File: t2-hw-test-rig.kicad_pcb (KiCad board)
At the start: 2 copper layers, 101.6 x 76.2 mm, 0 parts

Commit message: on to layout! and what an adventure it will be...
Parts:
- added C101: 10uF, tm-kicad-lib:SMD-0805-C, F.Cu at (25.1, 169.8)
- added C102: 100nF, tm-kicad-lib:SMD-0402-C, F.Cu at (143.9, 175.5)
- added C103: 100nF, tm-kicad-lib:SMD-0402-C, F.Cu at (141.2, 170.5)
- added C104: 100nF, tm-kicad-lib:SMD-0402-C, F.Cu at (91.8, 175.5)
- added C105: 100nF, tm-kicad-lib:SMD-0402-C, F.Cu at (126.5, 175.5)
- added C201: 100pF, tm-kicad-lib:SMD-0402-C, F.Cu at (89.2, 164.7)
- added C202: 100nF, tm-kicad-lib:SMD-0402-C, F.Cu at (68.6, 132.1)
- added C203: 100nF, tm-kicad-lib:SMD-0402-C, F.Cu at (173.6, 170.5)
- added C204: 100pF, tm-kicad-lib:SMD-0402-C, F.Cu at (105.2, 170.5)
- added C205: 10uF, tm-kicad-lib:SMD-0805-C, F.Cu at (17.4, 164.7)
- added C206: 10uF, tm-kicad-lib:SMD-0805-C, F.Cu at (16.6, 169.8)
- added C207: 100pF, tm-kicad-lib:SMD-0402-C, F.Cu at (84.1, 159.9)
- added C208: 18pF, tm-kicad-lib:SMD-0402-C, F.Cu at (66.7, 159.9)
- added C209: 100nF, tm-kicad-lib:SMD-0402-C, F.Cu at (93.4, 164.7)
- added C210: 18pF, tm-kicad-lib:SMD-0402-C, F.Cu at (42.8, 164.7)
- added C211: 100nF, tm-kicad-lib:SMD-0402-C, F.Cu at (55.1, 159.9)
- added C212: 100nF, tm-kicad-lib:SMD-0402-C, F.Cu at (49.3, 159.9)
- added C213: 10uF, tm-kicad-lib:SMD-0805-C, F.Cu at (29.3, 169.8)
- added C214: 100nF, tm-kicad-lib:SMD-0402-C, F.Cu at (43.5, 159.9)
- added C215: 100nF, tm-kicad-lib:SMD-0402-C, F.Cu at (38.5, 164.7)
- added C216: 10uF, tm-kicad-lib:SMD-0805-C, F.Cu at (37.7, 169.8)
- added C217: 100nF, tm-kicad-lib:SMD-0402-C, F.Cu at (57.0, 175.5)
- added C218: 10uF, tm-kicad-lib:SMD-0805-C, F.Cu at (20.8, 169.8)
- added C219: 10uF, tm-kicad-lib:SMD-0805-C, F.Cu at (116.8, 163.5)
- added C220: 1uF, tm-kicad-lib:SMD-0402-C, F.Cu at (63.8, 164.7)
- added C221: 1uF, tm-kicad-lib:SMD-0402-C, F.Cu at (107.3, 159.9)
- added C222: 1uF DNP, tm-kicad-lib:SMD-0402, F.Cu at (113.0, 159.9)
- added C223: 1uF DNP, tm-kicad-lib:SMD-0402, F.Cu at (118.8, 159.9)
- added C301: 10pF, tm-kicad-lib:SMD-0402-C, F.Cu at (87.6, 117.7)
- added C302: 100nF, tm-kicad-lib:SMD-0402-C, F.Cu at (86.0, 175.5)
- added C303: 100nF, tm-kicad-lib:SMD-0402-C, F.Cu at (101.5, 159.9)
- added C304: 10pF, tm-kicad-lib:SMD-0402-C, F.Cu at (89.5, 117.7)
- added C305: 100nF, tm-kicad-lib:SMD-0402-C, F.Cu at (134.0, 170.5)
- added C306: 1uF, tm-kicad-lib:SMD-0402-C, F.Cu at (138.1, 175.5)
- added C307: 100nF, tm-kicad-lib:SMD-0402-C, F.Cu at (28.0, 175.5)
- added C308: 10uF, tm-kicad-lib:SMD-0805-C, F.Cu at (41.9, 169.8)
- added C309: 10uF, tm-kicad-lib:SMD-0805-C, F.Cu at (46.1, 169.8)
- added C310: 100nF, tm-kicad-lib:SMD-0402-C, F.Cu at (55.4, 164.7)
- added C311: 100nF, tm-kicad-lib:SMD-0402-C, F.Cu at (101.8, 164.7)
- added C312: 10uF, tm-kicad-lib:SMD-0805-C, F.Cu at (121.0, 163.5)
- added C313: 100nF, tm-kicad-lib:SMD-0402-C, F.Cu at (148.4, 170.5)
- added C314: 100nF, tm-kicad-lib:SMD-0402-C, F.Cu at (53.4, 169.9)
- added C401: 100nF, tm-kicad-lib:SMD-0402-C, F.Cu at (108.8, 170.5)
- added C402: 100nF, tm-kicad-lib:SMD-0402-C, F.Cu at (148.0, 90.2)
- added C403: 100nF, tm-kicad-lib:SMD-0402-C, F.Cu at (97.6, 175.5)
- added C404: 100nF, tm-kicad-lib:SMD-0402-C, F.Cu at (147.3, 86.4)
- added C405: 100pF, tm-kicad-lib:SMD-0402-C, F.Cu at (115.0, 175.5)
- added C406: 100pF, tm-kicad-lib:SMD-0402-C, F.Cu at (147.3, 85.1)
- added C407: 100nF, tm-kicad-lib:SMD-0402-C, F.Cu at (106.0, 162.2)
- added C408: 100nF, tm-kicad-lib:SMD-0402-C, F.Cu at (80.7, 164.7)
- added C409: 100nF, tm-kicad-lib:SMD-0402-C, F.Cu at (76.5, 164.7)
- added C410: 100nF, tm-kicad-lib:SMD-0402-C, F.Cu at (84.9, 164.7)
- added C411: 100pF, tm-kicad-lib:SMD-0402-C, F.Cu at (62.8, 175.5)
- added C412: 100pF, tm-kicad-lib:SMD-0402-C, F.Cu at (132.3, 175.5)
- added C413: 100nF, tm-kicad-lib:SMD-0402-C, F.Cu at (45.4, 175.5)
- added C414: 100nF, tm-kicad-lib:SMD-0402-C, F.Cu at (51.2, 164.7)
- added C415: 100pF, tm-kicad-lib:SMD-0402-C, F.Cu at (39.6, 175.5)
- added C501: 100nF, tm-kicad-lib:SMD-0402-C, F.Cu at (137.6, 170.5)
- added C502: 100nF, tm-kicad-lib:SMD-0402-C, F.Cu at (130.4, 170.5)
- added C503: 100pF, tm-kicad-lib:SMD-0402-C, F.Cu at (22.2, 175.5)
- added C504: 100nF, tm-kicad-lib:SMD-0402-C, F.Cu at (16.4, 175.5)
- added C505: 100nF, tm-kicad-lib:SMD-0402-C, F.Cu at (109.2, 175.5)
- added C506: 100pF, tm-kicad-lib:SMD-0402-C, F.Cu at (72.3, 164.7)
- added C507: 100nF, tm-kicad-lib:SMD-0402-C, F.Cu at (60.9, 159.9)
- added C508: 100nF, tm-kicad-lib:SMD-0402-C, F.Cu at (33.8, 175.5)
- added C509: 100pF, tm-kicad-lib:SMD-0402-C, F.Cu at (68.1, 164.7)
- added D201: PRTR5V0U2X,215, tm-kicad-lib:PRTR5V0U2X,215, F.Cu at (77.7, 131.3)
- added D202: PRTR5V0U2X,215, tm-kicad-lib:PRTR5V0U2X,215, F.Cu at (74.4, 131.3)
- added D203: PRTR5V0U2X,215, tm-kicad-lib:PRTR5V0U2X,215, F.Cu at (73.9, 83.8)
- added D301: BLUE, LEDs:LED-0603, F.Cu at (114.3, 144.8)
- added D302: YELLOW, LEDs:LED-0603, F.Cu at (120.7, 144.8)
- added D303: GREEN, LEDs:LED-0603, F.Cu at (127.0, 144.8)
- added D304: RED, LEDs:LED-0603, F.Cu at (133.3, 144.8)
- added H101: M2.5, tm-kicad-lib:MountingHole_2-5mm, F.Cu at (147.3, 132.1)
- added H102: M2.5, tm-kicad-lib:MountingHole_2-5mm, F.Cu at (83.8, 78.7)
- added H103: M2.5, tm-kicad-lib:MountingHole_2-5mm, F.Cu at (147.3, 78.7)
- added H104: M2.5, tm-kicad-lib:MountingHole_2-5mm, F.Cu at (94.1, 118.9)
- added H105: M2.5, tm-kicad-lib:MountingHole_2-5mm, F.Cu at (53.3, 78.7)
- added H106: M2.5, tm-kicad-lib:MountingHole_2-5mm, F.Cu at (53.3, 149.9)
- added J101: CONN_01X02, Pin_Headers:Pin_Header_Straight_1x02, F.Cu at (54.0, 92.1)
- added J102: BARREL_JACK, Connect:BARREL_JACK, F.Cu at (61.0, 82.5)
- added J103: CONN_01X02, Pin_Headers:Pin_Header_Straight_1x02, F.Cu at (67.9, 88.3)
- added J201: MICROUSB-TH, tm-kicad-lib:Seeed-USB-Micro-320010028, F.Cu at (73.7, 77.5)
- added J202: CONN_01X02, Pin_Headers:Pin_Header_Straight_1x02, F.Cu at (78.1, 83.2)
- added J203: USB_A_2_stack, tm-kicad-lib:Molex-0672983090, F.Cu at (63.7, 138.2)
- added J204: USB_A_TH, tm-kicad-lib:USB-A, F.Cu at (58.4, 125.5)
- added J301: CONN_02x05, 0.05", tm-kicad-lib:CONN_02x05_0.05in, F.Cu at (77.5, 122.6)
- added L201: BLM21PG221SN1D, tm-kicad-lib:SMD-0805-R, F.Cu at (66.0, 132.1)
- added L202: BLM21PG221SN1D, tm-kicad-lib:SMD-0805-R, F.Cu at (62.2, 130.2)
- added L301: 10uH, tm-kicad-lib:SMD-0603-R, F.Cu at (137.6, 162.2)
- added L401: 10uH, tm-kicad-lib:SMD-0603-R, F.Cu at (141.8, 162.2)
- added L402: 10uH, tm-kicad-lib:SMD-0603-R, F.Cu at (147.3, 88.3)
- added L403: 10uH, tm-kicad-lib:SMD-0603-R, F.Cu at (25.9, 164.7)
- added L404: 10uH, tm-kicad-lib:SMD-0603-R, F.Cu at (30.1, 164.7)
- added L405: 10uH, tm-kicad-lib:SMD-0603-R, F.Cu at (146.0, 162.2)
- added L501: 10uH, tm-kicad-lib:SMD-0603-R, F.Cu at (21.7, 164.7)
- added L502: 10uH, tm-kicad-lib:SMD-0603-R, F.Cu at (34.3, 164.7)
- added L503: 10uH, tm-kicad-lib:SMD-0603-R, F.Cu at (133.4, 162.2)
- added Q101: pMOS, Housings_SOT-23_SOT-143_TSOT-6:SOT-23, F.Cu at (69.2, 83.8)
- added Q401: CJ2302, Housings_SOT-23_SOT-143_TSOT-6:SOT-23, F.Cu at (128.5, 96.0)
- added Q402: CJ2302, Housings_SOT-23_SOT-143_TSOT-6:SOT-23, F.Cu at (134.6, 83.8)
- added Q403: CJ2302, Housings_SOT-23_SOT-143_TSOT-6:SOT-23, F.Cu at (137.9, 104.4)
- added Q404: CJ2302, Housings_SOT-23_SOT-143_TSOT-6:SOT-23, F.Cu at (104.4, 82.0)
- added R201: 100kR, tm-kicad-lib:SMD-0402-R, F.Cu at (80.2, 175.5)
- added R202: 100kR, tm-kicad-lib:SMD-0402-R, F.Cu at (155.6, 170.5)
- added R203: 0R DNP, tm-kicad-lib:SMD-0603, F.Cu at (70.5, 128.3)
- added R204: 0R DNP, tm-kicad-lib:SMD-0603, F.Cu at (50.4, 169.8)
- added R205: 100kR, tm-kicad-lib:SMD-0402-R, F.Cu at (68.6, 175.5)
- added R206: 100kR, tm-kicad-lib:SMD-0402-R, F.Cu at (78.3, 159.9)
- added R207: 10kR, tm-kicad-lib:SMD-0402-R, F.Cu at (126.8, 170.5)
- added R208: 10kR, tm-kicad-lib:SMD-0402-R, F.Cu at (97.6, 164.7)
- added R209: 2.7kR 1%, tm-kicad-lib:SMD-0402-R, F.Cu at (124.6, 159.9)
- added R210: 1MR, tm-kicad-lib:SMD-0402-R, F.Cu at (59.6, 164.7)
- added R211: 1MR, tm-kicad-lib:SMD-0402-R, F.Cu at (31.9, 159.9)
- added R212: 1MR, tm-kicad-lib:SMD-0402-R, F.Cu at (112.4, 170.5)
- added R213: 1MR, tm-kicad-lib:SMD-0402-R, F.Cu at (72.5, 159.9)
- added R301: 1kR, tm-kicad-lib:SMD-0402-R, F.Cu at (103.4, 175.5)
- added R302: 330R, tm-kicad-lib:SMD-0402-R, F.Cu at (170.0, 170.5)
- added R303: 120R, tm-kicad-lib:SMD-0402-R, F.Cu at (149.7, 175.5)
- added R304: 1kR, tm-kicad-lib:SMD-0402-R, F.Cu at (74.4, 175.5)
- added R305: 10kR, tm-kicad-lib:SMD-0402-R, F.Cu at (110.3, 162.2)
- added R306: 10kR, tm-kicad-lib:SMD-0402-R, F.Cu at (153.2, 166.4)
- added R307: 10kR, tm-kicad-lib:SMD-0402-R, F.Cu at (152.0, 170.5)
- added R308: 1kR, tm-kicad-lib:SMD-0402-R, F.Cu at (51.2, 175.5)
- added R309: 1kR, tm-kicad-lib:SMD-0402-R, F.Cu at (162.8, 170.5)
- added R310: 10kR, tm-kicad-lib:SMD-0402-R, F.Cu at (95.7, 159.9)
- added R401: 10kR, tm-kicad-lib:SMD-0402-R, F.Cu at (47.0, 164.7)
- added R402: 10kR, tm-kicad-lib:SMD-0402-R, F.Cu at (37.7, 159.9)
- added R403: 20mR 1%, Resistors_SMD:R_1206, F.Cu at (132.1, 96.5)
- added R404: 20mR 1%, Resistors_SMD:R_1206, F.Cu at (138.4, 82.5)
- added R405: 10kR, tm-kicad-lib:SMD-0402-R, F.Cu at (26.1, 159.9)
- added R406: 10kR, tm-kicad-lib:SMD-0402-R, F.Cu at (120.8, 175.5)
- added R407: 20mR 1%, Resistors_SMD:R_1206, F.Cu at (138.4, 100.3)
- added R408: 20mR 1%, Resistors_SMD:R_1206, F.Cu at (108.0, 82.5)
- added R409: 20mR 1%, Resistors_SMD:R_1206, F.Cu at (59.7, 99.7)
- added RN501: ACASA100221002P100, tm-kicad-lib:ACAS0612, F.Cu at (128.9, 83.8)
- added RN502: ACASA100221002P100, tm-kicad-lib:ACAS0612, F.Cu at (117.5, 109.9)
- added RN503: ACASA100221002P100, tm-kicad-lib:ACAS0612, F.Cu at (129.5, 110.9)
- added RN504: ACASA100221002P100, tm-kicad-lib:ACAS0612, F.Cu at (120.7, 90.2)
- added SW301: Switch_DPST, tm-kicad-lib:SPST-TH, F.Cu at (81.3, 144.8)
- added SW302: Switch_DPST, tm-kicad-lib:SPST-TH, F.Cu at (104.1, 144.8)
- added TP301: 0932-0-15-20-77-14-11-0, tm-kicad-lib:0932-0-15-20-77-14-11-0, F.Cu at (88.9, 78.7)
- added TP302: 0932-0-15-20-77-14-11-0, tm-kicad-lib:0932-0-15-20-77-14-11-0, F.Cu at (96.5, 78.7)
- added TP303: 0932-0-15-20-77-14-11-0, tm-kicad-lib:0932-0-15-20-77-14-11-0, F.Cu at (101.6, 78.7)
- added TP304: 0932-0-15-20-77-14-11-0, tm-kicad-lib:0932-0-15-20-77-14-11-0, F.Cu at (124.2, 82.8)
- added TP305: 0932-0-15-20-77-14-11-0, tm-kicad-lib:0932-0-15-20-77-14-11-0, F.Cu at (99.1, 78.7)
- added TP306: 0932-0-15-20-77-14-11-0, tm-kicad-lib:0932-0-15-20-77-14-11-0, F.Cu at (104.1, 78.7)
- added TP307: 0932-0-15-20-77-14-11-0, tm-kicad-lib:0932-0-15-20-77-14-11-0, F.Cu at (106.7, 78.7)
- added TP308: 0932-0-15-20-77-14-11-0, tm-kicad-lib:0932-0-15-20-77-14-11-0, F.Cu at (94.0, 78.7)
- added TP309: 0932-0-15-20-77-14-11-0, tm-kicad-lib:0932-0-15-20-77-14-11-0, F.Cu at (91.4, 78.7)
- added TP310: 0932-0-15-20-77-14-11-0, tm-kicad-lib:0932-0-15-20-77-14-11-0, F.Cu at (134.6, 78.7)
- added TP311: 0932-0-15-20-77-14-11-0, tm-kicad-lib:0932-0-15-20-77-14-11-0, F.Cu at (137.2, 78.7)
- added TP312: 0932-0-15-20-77-14-11-0, tm-kicad-lib:0932-0-15-20-77-14-11-0, F.Cu at (124.5, 78.7)
- added TP313: 0932-0-15-20-77-14-11-0, tm-kicad-lib:0932-0-15-20-77-14-11-0, F.Cu at (121.9, 78.7)
- added TP314: 0932-0-15-20-77-14-11-0, tm-kicad-lib:0932-0-15-20-77-14-11-0, F.Cu at (127.0, 78.7)
- added TP315: 0932-0-15-20-77-14-11-0, tm-kicad-lib:0932-0-15-20-77-14-11-0, F.Cu at (129.5, 78.7)
- added TP316: 0932-0-15-20-77-14-11-0, tm-kicad-lib:0932-0-15-20-77-14-11-0, F.Cu at (132.1, 78.7)
- added TP317: 0932-0-15-20-77-14-11-0, tm-kicad-lib:0932-0-15-20-77-14-11-0, F.Cu at (113.8, 82.4)
- added TP318: 0932-0-15-20-77-14-11-0, tm-kicad-lib:0932-0-15-20-77-14-11-0, F.Cu at (116.8, 81.7)
- added TP319: 0932-0-15-20-77-14-11-0, tm-kicad-lib:0932-0-15-20-77-14-11-0, F.Cu at (119.4, 78.7)
- added TP321: 0932-0-15-20-77-14-11-0, tm-kicad-lib:0932-0-15-20-77-14-11-0, F.Cu at (123.4, 87.0)
- added TP324: 0932-0-15-20-77-14-11-0, tm-kicad-lib:0932-0-15-20-77-14-11-0, F.Cu at (138.8, 90.2)
- added TP325: 0932-0-15-20-77-14-11-0, tm-kicad-lib:0932-0-15-20-77-14-11-0, F.Cu at (131.7, 116.2)
- added TP326: 0932-0-15-20-77-14-11-0, tm-kicad-lib:0932-0-15-20-77-14-11-0, F.Cu at (101.2, 117.3)
- added TP327: 0932-0-15-20-77-14-11-0, tm-kicad-lib:0932-0-15-20-77-14-11-0, F.Cu at (111.8, 78.7)
- added TP328: 0932-0-15-20-77-14-11-0, tm-kicad-lib:0932-0-15-20-77-14-11-0, F.Cu at (142.2, 78.7)
- added TP401: 0932-0-15-20-77-14-11-0, tm-kicad-lib:0932-0-15-20-77-14-11-0, F.Cu at (135.6, 97.2)
- added TP402: 0932-0-15-20-77-14-11-0, tm-kicad-lib:0932-0-15-20-77-14-11-0, F.Cu at (139.7, 78.7)
- added TP403: 0932-0-15-20-77-14-11-0, tm-kicad-lib:0932-0-15-20-77-14-11-0, F.Cu at (138.2, 97.2)
- added TP404: 0932-0-15-20-77-14-11-0, tm-kicad-lib:0932-0-15-20-77-14-11-0, F.Cu at (109.2, 78.7)
- added TP503: 0932-0-15-20-77-14-11-0, tm-kicad-lib:0932-0-15-20-77-14-11-0, F.Cu at (113.1, 98.9)
- added TP504: 0932-0-15-20-77-14-11-0, tm-kicad-lib:0932-0-15-20-77-14-11-0, F.Cu at (104.6, 125.3)
- added TP505: 0932-0-15-20-77-14-11-0, tm-kicad-lib:0932-0-15-20-77-14-11-0, F.Cu at (120.8, 86.5)
- added TP507: 0932-0-15-20-77-14-11-0, tm-kicad-lib:0932-0-15-20-77-14-11-0, F.Cu at (140.3, 110.7)
- added TP509: 0932-0-15-20-77-14-11-0, tm-kicad-lib:0932-0-15-20-77-14-11-0, F.Cu at (136.3, 90.2)
- added TP510: TP, tm-kicad-lib:Testpoint, F.Cu at (113.3, 92.7)
- added U101: MAX6102, Housings_SOT-23_SOT-143_TSOT-6:SOT-23, F.Cu at (90.9, 113.4)
- added U102: XC6206P332MR-G, Housings_SOT-23_SOT-143_TSOT-6:SOT-23, F.Cu at (78.7, 91.4)
- added U201: AIC1528-0PSTR, tm-kicad-lib:SOP-8, F.Cu at (66.7, 127.6)
- added U202: FE1.1, tm-kicad-lib:CY7C65634-48AXCT, F.Cu at (67.9, 113.7)
- added U301: ATSAMD21J18A-MUT, Housings_DFN_QFN:QFN-64-1EP_9x9mm_Pitch0.5mm, F.Cu at (81.6, 112.1)
- added U302: AAT4610, Housings_SOT-23_SOT-143_TSOT-6:SOT-23-5, F.Cu at (59.7, 104.8)
- added U303: AAT4610, Housings_SOT-23_SOT-143_TSOT-6:SOT-23-5, F.Cu at (56.0, 104.8)
- added U401: MAX9919FASA+, SMD_Packages:SOIC-8-N, F.Cu at (130.8, 101.6)
- added U402: MAX9919FASA+, SMD_Packages:SOIC-8-N, F.Cu at (142.2, 86.4)
- added U403: MAX9919FASA+, SMD_Packages:SOIC-8-N, F.Cu at (143.5, 101.6)
- added U404: MAX9919FASA+, SMD_Packages:SOIC-8-N, F.Cu at (106.7, 87.6)
- added U405: MAX9919FASA+, SMD_Packages:SOIC-8-N, F.Cu at (66.0, 101.0)
- added U501: TSV324IDT, SMD_Packages:SOIC-14_N, F.Cu at (129.5, 90.2)
- added U502: TSV324IDT, SMD_Packages:SOIC-14_N, F.Cu at (123.8, 110.5)
- added U503: TSV324IDT, SMD_Packages:SOIC-14_N, F.Cu at (119.4, 95.9)
- added X201: 12MHz, tm-kicad-lib:Seeed-xtal-12MHz, F.Cu at (73.0, 119.4)
- added X301: FC-135, tm-kicad-lib:FC-135, F.Cu at (88.5, 119.3)
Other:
- board size 101.6 x 76.2 mm -> 99.1 x 76.2 mm

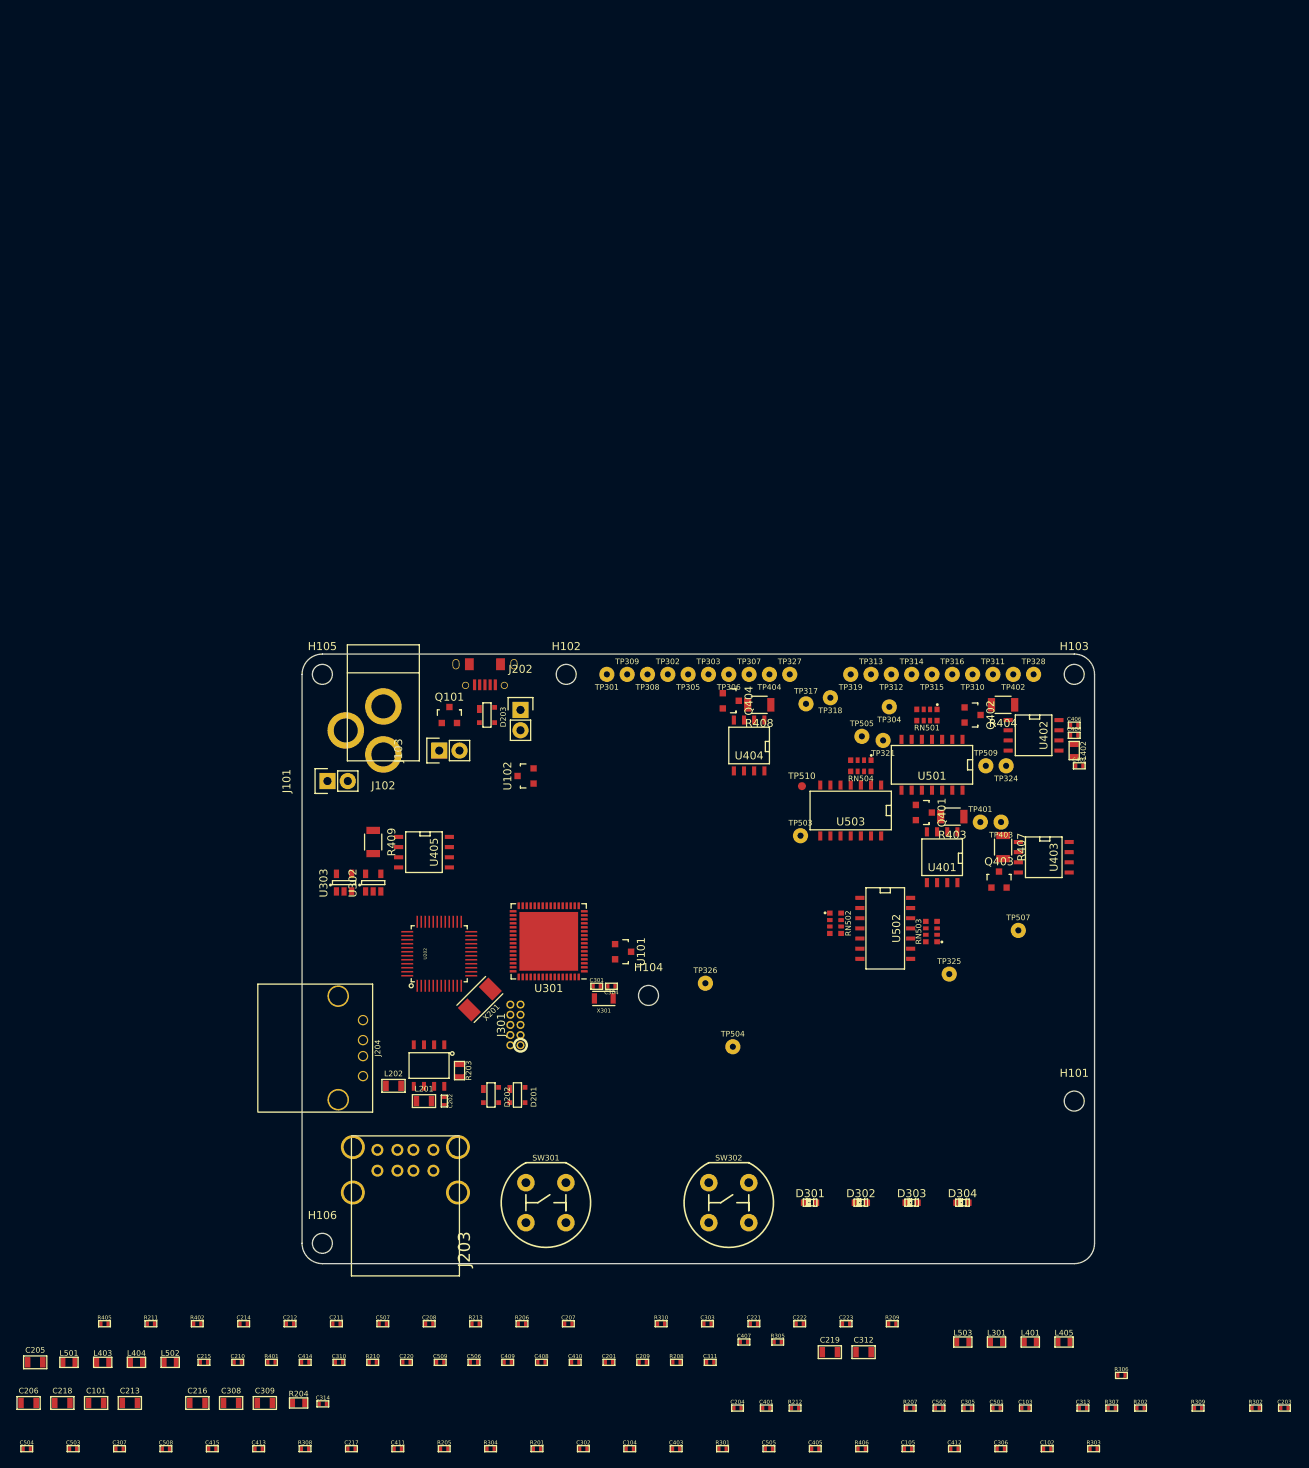
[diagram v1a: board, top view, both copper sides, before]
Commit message: significant progress on placement, sch changes for adc routing
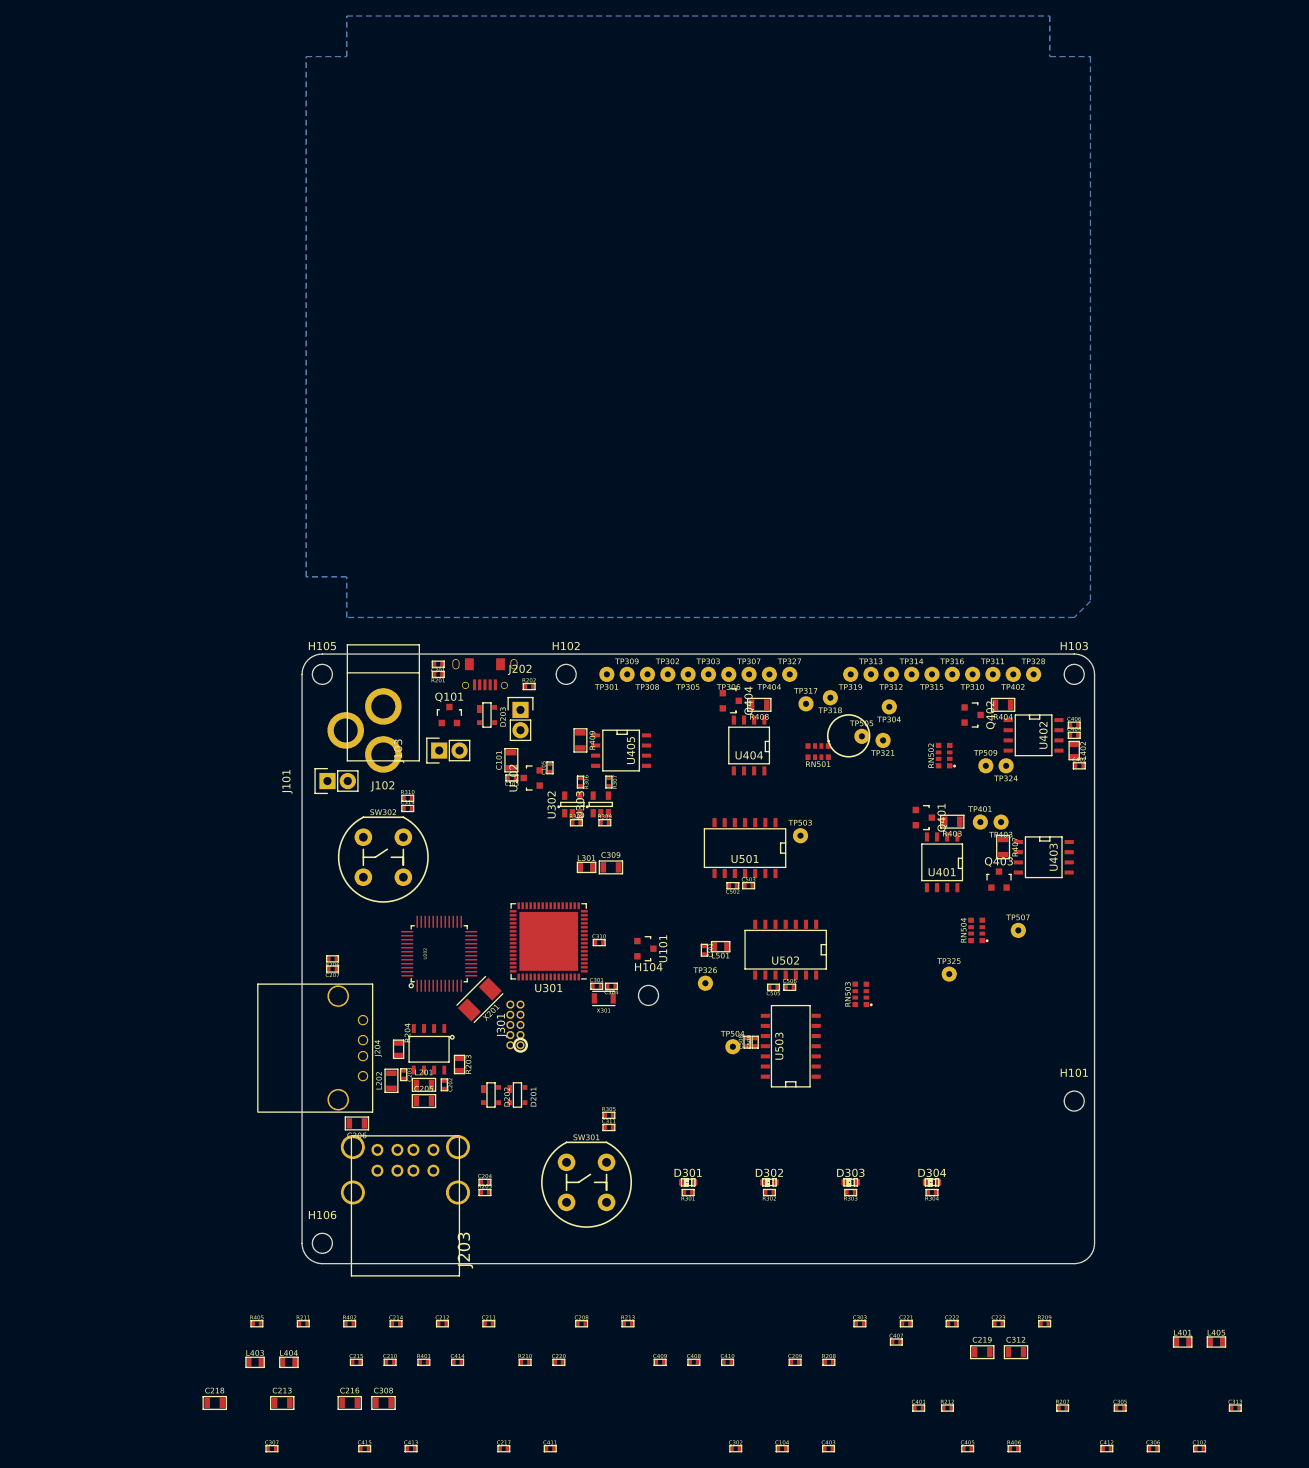
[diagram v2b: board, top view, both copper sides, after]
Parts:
- removed C504, C507: 100nF, tm-kicad-lib:SMD-0402-C
- removed L502, L503: 10uH, tm-kicad-lib:SMD-0603-R
- removed TP510: TP, tm-kicad-lib:Testpoint
- R403, R404, R407, R408, R409: footprint Resistors_SMD:R_1206 -> tm-kicad-lib:SMD-0805-R
- moved R202 118.2 mm to (79.2, 80.3)
- moved C203 117.7 mm to (63.5, 128.8), turned to 270 degrees
- moved C503 109.9 mm to (106.6, 105.2)
- moved R309 104.2 mm to (88.6, 97.3)
- moved C103 101.6 mm to (77.0, 91.7), turned to 180 degrees
- moved R306 100.4 mm to (85.6, 92.2), turned to 270 degrees
- moved R307 100.4 mm to (89.2, 92.2), turned to 270 degrees
- moved R201 97.6 mm to (67.8, 78.7), turned to 180 degrees
- moved L501 96.6 mm to (103.1, 112.8), turned to 180 degrees
- moved C105 96.2 mm to (81.8, 90.4), turned to 90 degrees
- moved C101 95.7 mm to (77.0, 89.5), turned to 90 degrees
- moved C201 89.8 mm to (67.8, 77.5), turned to 180 degrees
- moved C508 88.7 mm to (106.4, 124.7), turned to 90 degrees
- moved R308 85.3 mm to (85.1, 97.3)
- moved C309 79.7 mm to (89.4, 102.9)
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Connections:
- C502 pad 1: /OP AMPS/VDD_OPAMP0 -> /OP AMPS/VDD_OPAMPS
- C503 pad 1: /OP AMPS/VDD_OPAMP0 -> /OP AMPS/VDD_OPAMPS
- C505 pad 1: /OP AMPS/VDD_OPAMP1 -> /OP AMPS/VDD_OPAMPS
- C506 pad 1: /OP AMPS/VDD_OPAMP1 -> /OP AMPS/VDD_OPAMPS
- C508 pad 1: /OP AMPS/VDD_OPAMP2 -> /OP AMPS/VDD_OPAMPS
- C509 pad 1: /OP AMPS/VDD_OPAMP2 -> /OP AMPS/VDD_OPAMPS
- L501 pad 1: /OP AMPS/VDD_OPAMP0 -> /OP AMPS/VDD_OPAMPS
- RN501 pad 1: UUT_33PA -> UUT_33CP
- RN501 pad 7: /OP AMPS/33PA_DIV -> /OP AMPS/33CP_DIV
- RN501 pad 8: /OP AMPS/33PA_DIV -> /OP AMPS/33CP_DIV
- RN502 pad 1: UUT_33MT -> UUT_5V
- RN502 pad 3: UUT_33CP -> UUT_33PA
- RN502 pad 5: /OP AMPS/33CP_DIV -> /OP AMPS/33PA_DIV
- RN502 pad 6: /OP AMPS/33CP_DIV -> /OP AMPS/33PA_DIV
- RN502 pad 7: /OP AMPS/33MT_DIV -> /OP AMPS/5V_DIV
- RN502 pad 8: /OP AMPS/33MT_DIV -> /OP AMPS/5V_DIV
- RN503 pad 1: UUT_5VUSB0 -> UUT_5VUSB1
- RN503 pad 3: UUT_5VUSB1 -> UUT_5VUSB0
- RN503 pad 5: /OP AMPS/5VUSB1_DIV -> /OP AMPS/5VUSB0_DIV
- RN503 pad 6: /OP AMPS/5VUSB1_DIV -> /OP AMPS/5VUSB0_DIV
- RN503 pad 7: /OP AMPS/5VUSB0_DIV -> /OP AMPS/5VUSB1_DIV
- RN503 pad 8: /OP AMPS/5VUSB0_DIV -> /OP AMPS/5VUSB1_DIV
- RN504 pad 2: UUT_5V -> UUT_33MT
- RN504 pad 6: /OP AMPS/5V_DIV -> /OP AMPS/33MT_DIV
- RN504 pad 7: /OP AMPS/5V_DIV -> /OP AMPS/33MT_DIV
- U301 pad 10: I_PB33 -> 33PB_DIV_BUFF
- U301 pad 11: I_UUT -> 12_BUFF
- U301 pad 12: 5V_DIV_BUFF -> 33CP_DIV_BUFF
- U301 pad 13: 5VUSB0_DIV_BUFF -> I_USB0
- U301 pad 14: 5VUSB1_DIV_BUFF -> I_USB1
- U301 pad 15: 33MT_DIV_BUFF -> 33PA_DIV_BUFF
- U301 pad 16: 33CP_DIV_BUFF -> 5V_DIV_BUFF
- U301 pad 5: I_USB0 -> I_UUT
- U301 pad 6: I_USB1 -> I_PA33
- U301 pad 61: 18_BUFF -> 5VUSB0_DIV_BUFF
- U301 pad 62: 12_BUFF -> 5VUSB1_DIV_BUFF
- U301 pad 63: 33PA_DIV_BUFF -> 33MT_DIV_BUFF
- U301 pad 64: 33PB_DIV_BUFF -> 18_BUFF
- U301 pad 9: I_PA33 -> I_PB33
- U501 pad 1: 33PA_DIV_MEAS -> 33CP_DIV_BUFF
- U501 pad 10: /OP AMPS/UUT_12 -> GND
- U501 pad 11: /OP AMPS/VDD_OPAMP0 -> /OP AMPS/VDD_OPAMPS
- U501 pad 12: /OP AMPS/UUT_18 -> /OP AMPS/UUT_12
- U501 pad 13: 18_BUFF -> 12_BUFF
- U501 pad 14: 18_BUFF -> 12_BUFF
- U501 pad 2: 33PA_DIV_MEAS -> 33CP_DIV_BUFF
- U501 pad 3: /OP AMPS/33PA_DIV -> /OP AMPS/33CP_DIV
- U501 pad 8: 12_BUFF -> Net-(U501-Pad8)
- U501 pad 9: 12_BUFF -> GND
- U502 pad 1: 33MT_DIV_BUFF -> 5V_DIV_BUFF
- U502 pad 10: /OP AMPS/5VUSB0_DIV -> /OP AMPS/5VUSB1_DIV
- U502 pad 11: /OP AMPS/VDD_OPAMP1 -> /OP AMPS/VDD_OPAMPS
- U502 pad 12: /OP AMPS/5VUSB1_DIV -> /OP AMPS/5VUSB0_DIV
- U502 pad 13: 5VUSB1_DIV_BUFF -> 5VUSB0_DIV_BUFF
- U502 pad 14: 5VUSB1_DIV_BUFF -> 5VUSB0_DIV_BUFF
- U502 pad 2: 33MT_DIV_BUFF -> 5V_DIV_BUFF
- U502 pad 3: /OP AMPS/33MT_DIV -> /OP AMPS/5V_DIV
- U502 pad 5: /OP AMPS/33CP_DIV -> /OP AMPS/33PA_DIV
- U502 pad 6: 33CP_DIV_BUFF -> 33PA_DIV_BUFF
- U502 pad 7: 33CP_DIV_BUFF -> 33PA_DIV_BUFF
- U502 pad 8: 5VUSB0_DIV_BUFF -> 5VUSB1_DIV_BUFF
- U502 pad 9: 5VUSB0_DIV_BUFF -> 5VUSB1_DIV_BUFF
- U503 pad 1: 5V_DIV_BUFF -> Net-(U503-Pad1)
- U503 pad 11: /OP AMPS/VDD_OPAMP2 -> /OP AMPS/VDD_OPAMPS
- U503 pad 12: GND -> /OP AMPS/UUT_18
- U503 pad 13: Net-(U503-Pad13) -> 18_BUFF
- U503 pad 14: Net-(U503-Pad13) -> 18_BUFF
- U503 pad 2: 5V_DIV_BUFF -> GND
- U503 pad 3: /OP AMPS/5V_DIV -> GND
- U503 pad 5: VREF -> /OP AMPS/33MT_DIV
- U503 pad 6: VREF_BUFF -> 33MT_DIV_BUFF
- U503 pad 7: VREF_BUFF -> 33MT_DIV_BUFF
- U503 pad 9: Net-(U503-Pad8) -> GND
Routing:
- added copper zone on B.Cu, net GND
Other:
- net class Default: clearance 0.2 -> 0.2032; trace_width 0.25 -> 0.2032
- rule trace_clearance: 0.2 -> 0.2032
- rule trace_min: 0.2 -> 0.2032

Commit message: usb refactor on sch and pcb, mechanical constraints on bcp
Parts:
- removed C203, C209, C211, C212, C214, C215, C217: 100nF, tm-kicad-lib:SMD-0402-C
- removed C204: 100pF, tm-kicad-lib:SMD-0402-C
- removed C205, C206, C213, C216, C218, C219: 10uF, tm-kicad-lib:SMD-0805-C
- removed C208, C210: 18pF, tm-kicad-lib:SMD-0402-C
- removed C220, C221: 1uF, tm-kicad-lib:SMD-0402-C
- removed C222, C223: 1uF DNP, tm-kicad-lib:SMD-0402
- removed D202: PRTR5V0U2X,215, tm-kicad-lib:PRTR5V0U2X,215
- removed L201, L202: BLM21PG221SN1D, tm-kicad-lib:SMD-0805-R
- removed R204: 0R DNP, tm-kicad-lib:SMD-0603
- removed R205: 100kR, tm-kicad-lib:SMD-0402-R
- removed R207, R208: 10kR, tm-kicad-lib:SMD-0402-R
- removed R209: 2.7kR 1%, tm-kicad-lib:SMD-0402-R
- removed R210, R211, R212, R213: 1MR, tm-kicad-lib:SMD-0402-R
- removed U201: AIC1528-0PSTR, tm-kicad-lib:SOP-8
- removed U202: FE1.1, tm-kicad-lib:CY7C65634-48AXCT
- removed X201: 12MHz, tm-kicad-lib:Seeed-xtal-12MHz
- added H107: M2.5, tm-kicad-lib:MountingHole_2-5mm, F.Cu at (134.6, 61.0)
- added H108: M2.5, tm-kicad-lib:MountingHole_2-5mm, F.Cu at (134.6, 149.9)
- added H109: M2.5, tm-kicad-lib:MountingHole_2-5mm, F.Cu at (71.1, 86.4)
- added H110: M2.5, tm-kicad-lib:MountingHole_2-5mm, F.Cu at (71.1, 149.9)
- added H111: M2.5, tm-kicad-lib:MountingHole_2-5mm, F.Cu at (134.6, 86.4)
- C202: value 100nF -> 100pF
- J203: value USB_A_2_stack -> MICROUSB-TH; footprint tm-kicad-lib:Molex-0672983090 -> tm-kicad-lib:Seeed-USB-Micro-320010028
- R203: value 0R DNP -> 100kR; footprint tm-kicad-lib:SMD-0603 -> tm-kicad-lib:SMD-0402-R
- U401, U402, U403, U404, U405: footprint SMD_Packages:SOIC-8-N -> tm-kicad-lib:SOIC-8-N-1EP
- moved D301 137.2 mm to (-38.1, 142.2)
- moved D302 137.2 mm to (-27.9, 142.2)
- moved D303 137.2 mm to (-17.8, 142.2)
- moved D304 137.2 mm to (-7.62, 142.2)
- moved R301 137.2 mm to (-38.1, 143.5)
- moved R302 137.2 mm to (-27.9, 143.5)
- moved R303 137.2 mm to (-17.8, 143.5)
- moved R304 137.2 mm to (-7.62, 143.5)
- moved SW301 98.2 mm to (-8.38, 116.6)
- moved C311 98.2 mm to (-5.59, 109.7)
- moved R305 98.2 mm to (-5.59, 108.2)
- moved J203 97.0 mm to (120.7, 59.7)
- moved J204 85.8 mm to (125.7, 72.4), turned to 90 degrees
- moved U301 54.4 mm to (27.8, 120.0)
- moved X301 54.4 mm to (34.7, 127.1)
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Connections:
- C202 pad 1: /USB/VBUS[1]_IN -> /USB/UUT_USB_PASSTHROUGH_SHELL
- D201 pad 2: /USB/USB_DD-[2] -> /USB/UUT_USB_D+
- D201 pad 3: /USB/USB_DD+[2] -> /USB/UUT_USB_D-
- D203 pad 2: /USB/UPSTREAM_USB_D+ -> SAM_USB_D+
- D203 pad 3: /USB/UPSTREAM_USB_D- -> SAM_USB_D-
- J201 pad 2: /USB/UPSTREAM_USB_D- -> SAM_USB_D-
- J201 pad 3: /USB/UPSTREAM_USB_D+ -> SAM_USB_D+
- J203 pad 1: /USB/VBUS[1] -> Net-(J203-Pad1)
- J203 pad 10: Net-(C204-Pad1) -> /USB/UUT_USB_PASSTHROUGH_SHELL
- J203 pad 11: Net-(C204-Pad1) -> /USB/UUT_USB_PASSTHROUGH_SHELL
- J203 pad 2: /USB/USB_DD-[1] -> /USB/UUT_USB_D-
- J203 pad 3: /USB/USB_DD+[1] -> /USB/UUT_USB_D+
- J203 pad 4: GND -> Net-(J203-Pad4)
- J203 pad 5: /USB/VBUS[2] -> GND
- J203 pad 6: /USB/USB_DD-[2] -> /USB/UUT_USB_PASSTHROUGH_SHELL
- J203 pad 7: /USB/USB_DD+[2] -> /USB/UUT_USB_PASSTHROUGH_SHELL
- J203 pad 8: GND -> /USB/UUT_USB_PASSTHROUGH_SHELL
- J203 pad 9: Net-(C204-Pad1) -> /USB/UUT_USB_PASSTHROUGH_SHELL
- R203 pad 1: +5V -> /USB/UUT_USB_PASSTHROUGH_SHELL
- R203 pad 2: /USB/VBUS[1]_IN -> GND
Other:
- board size 99.1 x 76.2 mm -> 86.4 x 94 mm

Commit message: packed parts in
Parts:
- moved R301 133.5 mm to (95.3, 149.7)
- moved D301 131.0 mm to (92.7, 149.7), turned to 180 degrees
- moved R302 129.8 mm to (101.7, 150.0)
- moved D302 127.3 mm to (99.2, 150.0), turned to 180 degrees
- moved R303 126.0 mm to (108.1, 149.7)
- moved D303 123.5 mm to (105.5, 149.7), turned to 180 degrees
- moved R304 122.2 mm to (114.4, 149.7)
- moved D304 119.7 mm to (111.8, 149.7), turned to 180 degrees
- moved C202 117.2 mm to (113.0, 61.0)
- moved R203 114.9 mm to (114.3, 61.0)
- moved D201 113.9 mm to (120.7, 67.3)
- moved L401 91.8 mm to (69.1, 161.3)
- moved C207 90.9 mm to (128.3, 62.2)
- moved R206 90.9 mm to (128.3, 61.0)
- moved C313 79.4 mm to (89.3, 156.2)
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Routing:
- removed copper zone on B.Cu, net GND
